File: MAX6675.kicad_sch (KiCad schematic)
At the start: 2 parts, among them U501 MAX6675

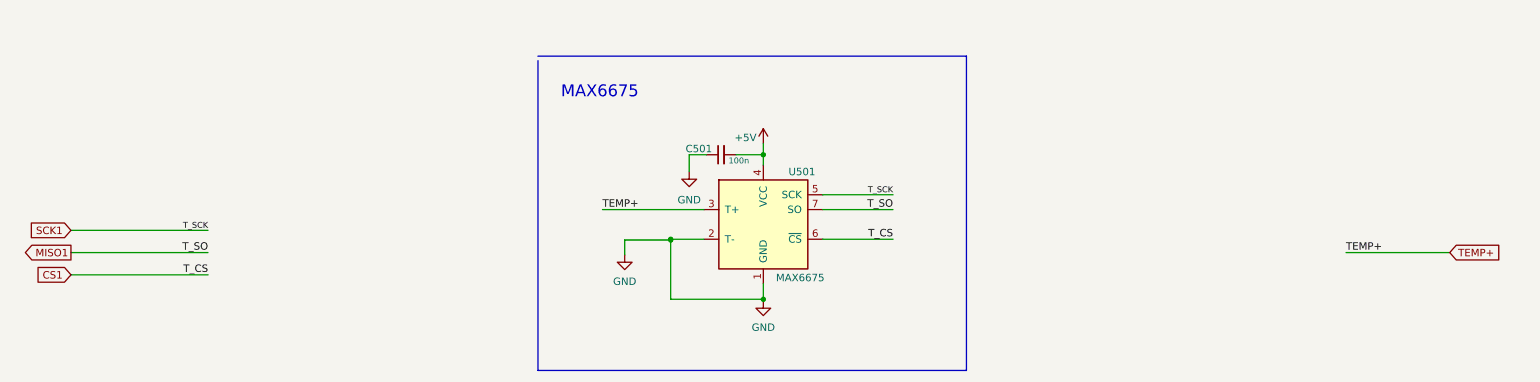
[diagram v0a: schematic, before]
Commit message: Added 24v to 5v SMPS, Reduced it to 2 Story, Used Small Relays
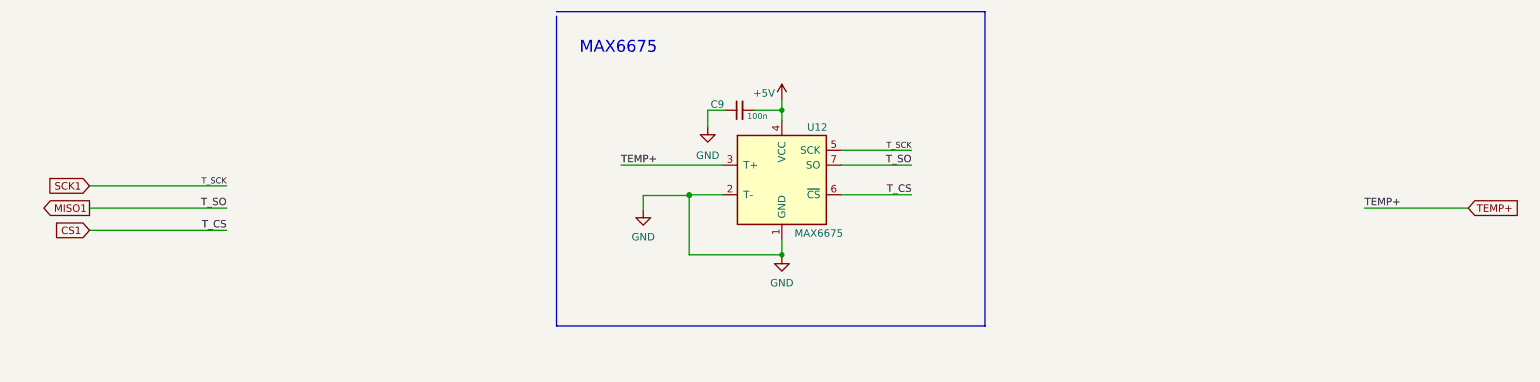
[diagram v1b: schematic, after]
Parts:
- removed C501: 100n, User_Capacitor_THT:C_Disc_D4.3mm_W1.9mm_P5.00mm, symbol Device:C_Small
- removed U501: MAX6675, Package_SO:SOIC-8_3.9x4.9mm_P1.27mm, symbol Sensor_Temperature:MAX31855KASA
- added C9: 100n, Capacitor_THT:C_Disc_D4.3mm_W1.9mm_P5.00mm, symbol Device:C_Small
- added U12: MAX6675, Package_SO:SOIC-8_3.9x4.9mm_P1.27mm, symbol Sensor_Temperature:MAX31855KASA
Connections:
- net +5V: now also C9.2, U12.4 (VCC)
- net CS1: now also U12.6 (~{CS})
- net GND: now also C9.1, U12.1 (GND), U12.2 (T-)
- net MISO1: now also U12.7 (SO)
- net SCK1: now also U12.5 (SCK)
- net TEMP+: now also U12.3 (T+)
